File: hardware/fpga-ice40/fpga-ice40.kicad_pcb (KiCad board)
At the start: 4 copper layers, 53.3 x 70.1 mm, 65 parts, among them J1 MicroSD_Molex_1040310811, J2 ProgHeader_iCE40, J3 ProgHeader_Flash_QSPI, J4 Conn_02x20_Odd_Even, J5 USB_B_Micro, U1 iCE40HX4K-TQ144, U2 IS42S16320F-6TL, U3 W25Q32JVSS, U4 W25Q32JVSS, U5 S25FL256SAGMFI01, U6 S25FL256SAGMFI01, U7 FT245RL

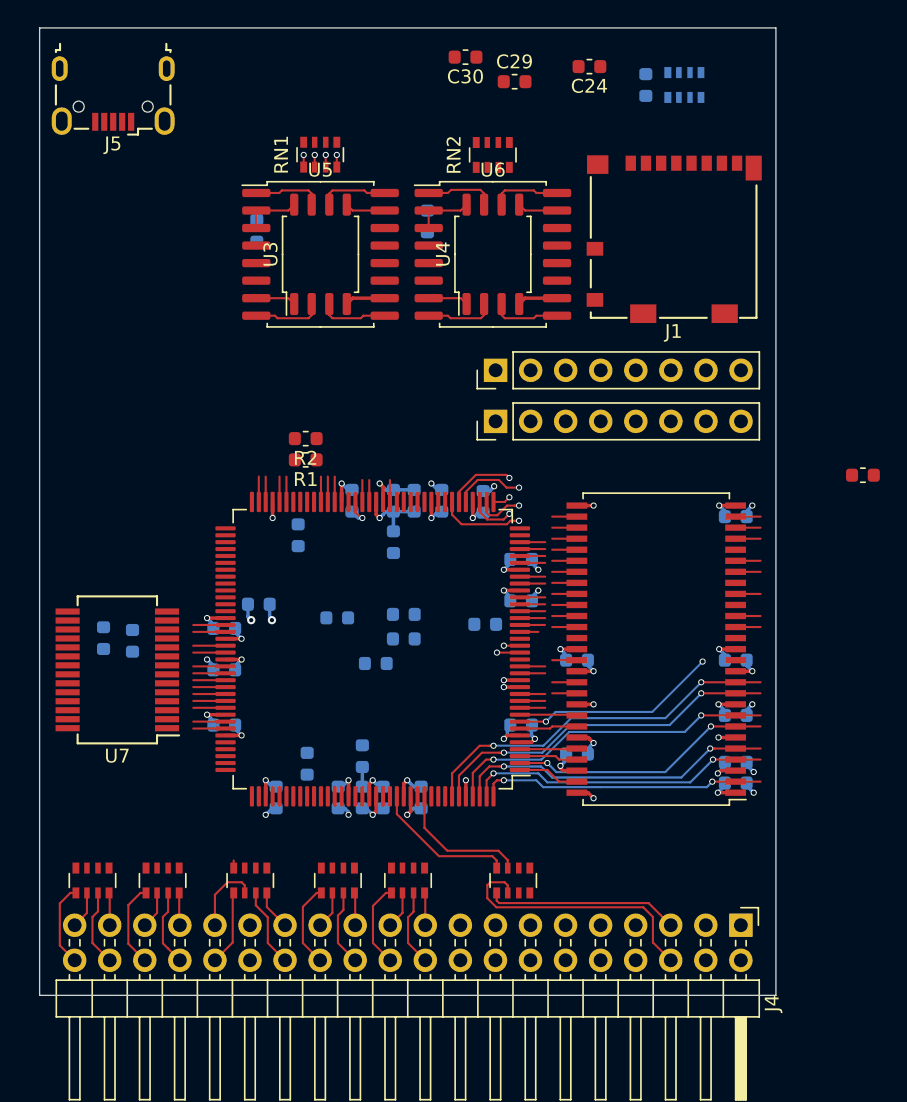
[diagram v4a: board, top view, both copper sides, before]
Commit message: Routing FPGA to SPI flash memory and USB interface
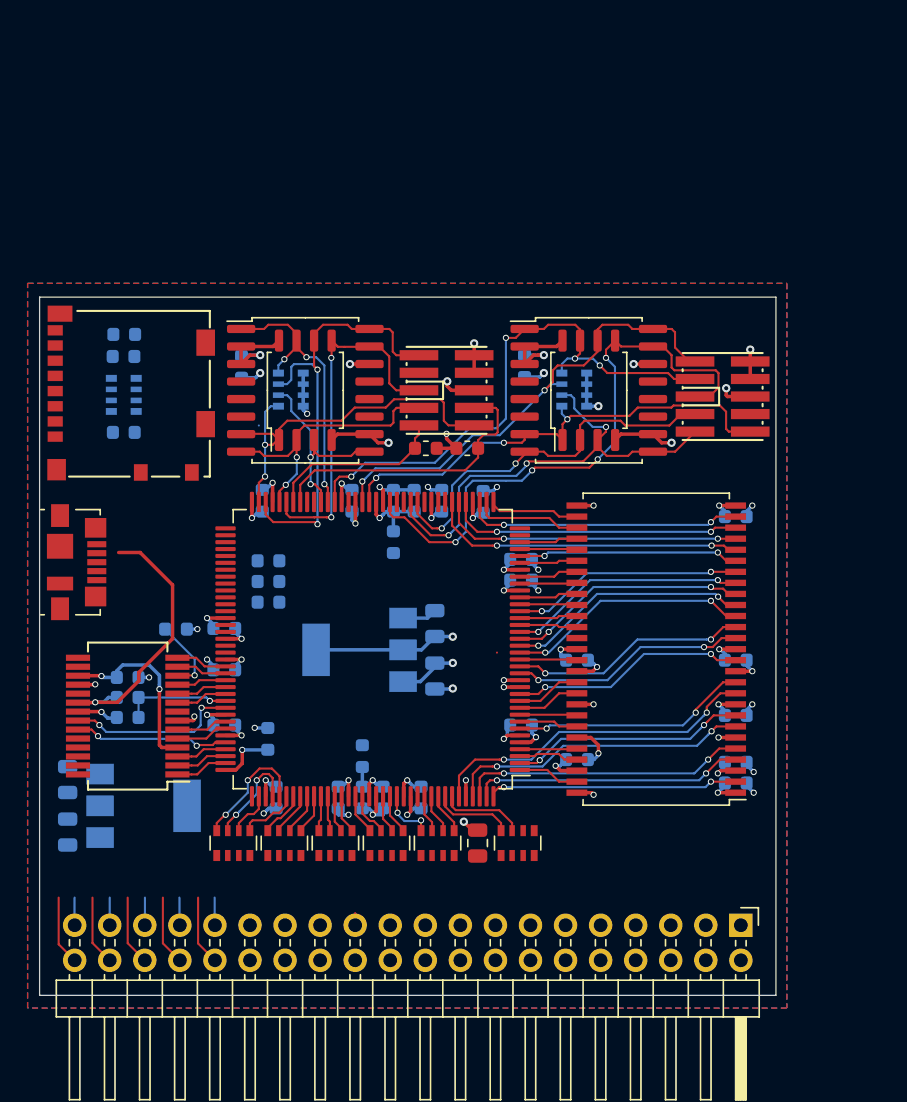
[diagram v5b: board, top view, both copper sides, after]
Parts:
- removed J2: ProgHeader_iCE40, Connector_PinHeader_2.54mm:PinHeader_1x08_P2.54mm_Vertical
- removed J3: ProgHeader_Flash_QSPI, Connector_PinHeader_2.54mm:PinHeader_1x08_P2.54mm_Vertical
- removed R5, R6, R7: 1R, Resistor_SMD:R_0603_1608Metric
- added C34: 10u, Capacitor_SMD:C_0805_2012Metric, B.Cu at (137.9, 104.5)
- added C35: 10u, Capacitor_SMD:C_0805_2012Metric, B.Cu at (137.9, 108.2)
- added C36: 10u, Capacitor_SMD:C_0805_2012Metric, F.Cu at (167.6, 109.0)
- added C37: 10u, Capacitor_SMD:C_0805_2012Metric, B.Cu at (164.5, 97.0)
- added C38: 10u, Capacitor_SMD:C_0805_2012Metric, B.Cu at (164.5, 93.2)
- added J6: Conn_02x05_Odd_Even, ng_conn:Samtec_FTSH-105-XX-X-DV, F.Cu at (165.3, 76.2)
- added J7: Conn_02x05_Odd_Even, ng_conn:Samtec_FTSH-105-XX-X-DV, F.Cu at (185.3, 76.7)
- added U8: AZ1117-1.2, Package_TO_SOT_SMD:SOT-223-3_TabPin2, B.Cu at (143.4, 106.3)
- added U9: AZ1117-1.2, Package_TO_SOT_SMD:SOT-223-3_TabPin2, B.Cu at (159.1, 95.0)
- C24, C30, RN1, RN2: moved to B.Cu
- C28, C29: value 10u -> 100n; moved to B.Cu
- J5: footprint Connector_USB:USB_Micro-B_Wuerth_629105150521 -> Connector_USB:USB_Micro-B_Molex_47346-0001
- R3: value 1R -> 6k8
- R4: value 1R -> 10k
- moved C29 50.9 mm to (152.4, 101.5), turned to 90 degrees
- moved J1 47.8 mm to (137.0, 76.5), turned to 270 degrees
- moved RN3 46.4 mm to (142.0, 76.6), turned to 0 degrees
- moved R8 45.4 mm to (142.0, 79.3), turned to 180 degrees
- moved C28 43.6 mm to (152.0, 84.2), turned to 90 degrees
- moved C24 38.9 mm to (142.0, 72.2), turned to 0 degrees
- moved J5 33.9 mm to (138.6, 88.7), turned to 270 degrees
- moved C30 32.9 mm to (141.9, 73.8), turned to 0 degrees
- moved R3 20.4 mm to (142.2, 98.5)
- moved RN2 18.0 mm to (174.6, 76.2), turned to 0 degrees
- moved RN1 17.2 mm to (154.1, 76.2), turned to 0 degrees
- moved R4 13.4 mm to (142.2, 100.0), turned to 180 degrees
- moved C23 12.6 mm to (171.0, 74.5)
- moved U4 12.1 mm to (175.7, 76.2)
- moved U6 12.1 mm to (175.7, 76.2)
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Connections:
- net N64_VCC renamed N64_3V3
- net Net-(R9-Pad2) renamed /USB_PWRENn
- C1 pad 1: VCCINT -> P1V2
- C10 pad 1: VCCIO1 -> P3V3
- C11 pad 1: VCCIO2 -> P3V3
- C12 pad 1: VCCIO2 -> P3V3
- C13 pad 1: VCCIO3 -> P3V3
- C14 pad 1: VCCIO3 -> P3V3
- C15 pad 1: P3V3_DRAM -> P3V3
- C16 pad 1: P3V3_DRAM -> P3V3
- C17 pad 1: P3V3_DRAM -> P3V3
- C18 pad 1: P3V3_DRAM -> P3V3
- C19 pad 1: P3V3_DRAM -> P3V3
- C2 pad 1: VCCINT -> P1V2
- C20 pad 1: P3V3_DRAM -> P3V3
- C21 pad 1: P3V3_DRAM -> P3V3
- C22 pad 1: P3V3_FLASH -> P3V3
- C23 pad 1: P3V3_FLASH -> P3V3
- C24 pad 1: P3V3_SD -> P3V3
- C27 pad 1: P3V3_FPGA -> P3V3
- C28 pad 1: P3V3_DRAM -> P3V3
- C29 pad 1: P3V3_FLASH -> VCC2V5
- C3 pad 1: VCCINT -> P1V2
- C30 pad 1: P3V3_SD -> P3V3
- C31 pad 1: VCCINT -> P1V2
- C32 pad 1: VCCINT -> P1V2
- C33 pad 1: Net-(C33-Pad1) -> /USB_VIO
- C4 pad 1: VCCINT -> P1V2
- C7 pad 1: VCCIO0 -> P3V3
- C8 pad 1: VCCIO0 -> P3V3
- C9 pad 1: VCCIO1 -> P3V3
- J1 pad 4: P3V3_SD -> P3V3
- R3 pad 1: VCCINT -> USB_VBUS
- R3 pad 2: P1V2 -> USB_DETn
- R4 pad 1: VCCIO0 -> USB_DETn
- R4 pad 2: P3V3 -> GND
- R8 pad 1: P3V3_SD -> P3V3
- RN1 pad 2: CONFIG_SCK -> CONFIG_IO2
- RN1 pad 3: CONFIG_IO2 -> CONFIG_SCK
- RN1 pad 5: P3V3_FLASH -> P3V3
- RN1 pad 6: P3V3_FLASH -> P3V3
- RN1 pad 7: P3V3_FLASH -> P3V3
- RN1 pad 8: P3V3_FLASH -> P3V3
- RN2 pad 2: FLASH_SCK -> FLASH_IO2
- RN2 pad 3: FLASH_IO2 -> FLASH_SCK
- RN2 pad 5: P3V3_FLASH -> P3V3
- RN2 pad 6: P3V3_FLASH -> P3V3
- RN2 pad 7: P3V3_FLASH -> P3V3
- RN2 pad 8: P3V3_FLASH -> P3V3
- RN3 pad 5: P3V3_SD -> P3V3
- RN3 pad 6: P3V3_SD -> P3V3
- RN3 pad 7: P3V3_SD -> P3V3
- RN3 pad 8: P3V3_SD -> P3V3
- U1 pad 10: Net-(U1-Pad10) -> DRAM_DQ10
- U1 pad 100: VCCIO1 -> P3V3
- U1 pad 101: Net-(U1-Pad101) -> FIFO_D7
- U1 pad 102: Net-(U1-Pad102) -> FIFO_D1
- U1 pad 104: N64_AD15_IC -> FIFO_RXFn
- U1 pad 105: N64_AD0_IC -> FIFO_D2
- U1 pad 106: N64_AD14_IC -> FIFO_D4
- U1 pad 107: N64_AD1_IC -> FIFO_D0
- U1 pad 11: Net-(U1-Pad11) -> DRAM_DQ9
- U1 pad 110: N64_AD13_IC -> N64_AD14_IC
- U1 pad 111: VCCINT -> P1V2
- U1 pad 112: N64_AD2_IC -> N64_AD0_IC
- U1 pad 113: N64_AD12_IC -> N64_AD15_IC
- U1 pad 114: N64_AD3_IC -> N64_AD1_IC
- U1 pad 115: N64_WRITEn_IC -> N64_AD13_IC
- U1 pad 116: N64_ALE_L_IC -> N64_AD2_IC
- U1 pad 117: N64_READn_IC -> N64_AD12_IC
- U1 pad 118: N64_ALE_H_IC -> N64_AD3_IC
- U1 pad 119: N64_AD11_IC -> N64_WRITEn_IC
- U1 pad 12: Net-(U1-Pad12) -> DRAM_DQ7
- U1 pad 120: N64_AD4_IC -> N64_ALE_L_IC
- U1 pad 121: N64_AD10_IC -> N64_READn_IC
- U1 pad 122: N64_AD5_IC -> N64_ALE_H_IC
- U1 pad 123: VCCIO0 -> P3V3
- U1 pad 124: N64_AD9_IC -> N64_AD11_IC
- U1 pad 125: N64_AD6_IC -> N64_AD4_IC
- U1 pad 128: N64_AD8_IC -> N64_AD10_IC
- U1 pad 129: N64_AD7_IC -> N64_AD5_IC
- U1 pad 130: N64_COLD_RESETn_IC -> N64_AD9_IC
- U1 pad 131: VCCIO0 -> P3V3
- U1 pad 134: N64_OS_EVENTn_IC -> N64_AD6_IC
- U1 pad 135: Net-(U1-Pad135) -> N64_AD8_IC
- U1 pad 136: Net-(U1-Pad136) -> N64_AD7_IC
- U1 pad 137: Net-(U1-Pad137) -> N64_COLD_RESETn_IC
- U1 pad 138: DRAM_DQ6 -> N64_OS_EVENTn_IC
- U1 pad 141: DRAM_DQ4 -> DRAM_DQ3
- U1 pad 15: DRAM_DQ9 -> DRAM_LDQM
- U1 pad 16: DRAM_DQ8 -> DRAM_WEn
- U1 pad 17: Net-(U1-Pad17) -> DRAM_DQ8
- U1 pad 18: Net-(U1-Pad18) -> DRAM_CASn
- U1 pad 19: Net-(U1-Pad19) -> DRAM_RASn
- U1 pad 2: DRAM_DQ3 -> DRAM_DQ4
- U1 pad 20: Net-(U1-Pad20) -> DRAM_CSn
- U1 pad 21: Net-(U1-Pad21) -> DRAM_BA0
- U1 pad 22: Net-(U1-Pad22) -> DRAM_UDQM
- U1 pad 23: Net-(U1-Pad23) -> DRAM_CLK
- U1 pad 24: Net-(U1-Pad24) -> DRAM_BA1
- U1 pad 25: Net-(U1-Pad25) -> DRAM_CKE
- U1 pad 26: Net-(U1-Pad26) -> DRAM_A12
- U1 pad 27: VCCINT -> P1V2
- U1 pad 28: Net-(U1-Pad28) -> DRAM_A11
- U1 pad 29: Net-(U1-Pad29) -> DRAM_A9
- U1 pad 30: VCCIO3 -> P3V3
- U1 pad 31: Net-(U1-Pad31) -> DRAM_A8
- U1 pad 32: Net-(U1-Pad32) -> DRAM_A10
- U1 pad 33: Net-(U1-Pad33) -> DRAM_A7
- U1 pad 34: Net-(U1-Pad34) -> DRAM_A6
- U1 pad 37: Net-(U1-Pad37) -> DRAM_A4
- U1 pad 38: Net-(U1-Pad38) -> DRAM_A5
- U1 pad 39: Net-(U1-Pad39) -> DRAM_A3
- U1 pad 40: VCCINT -> P1V2
- U1 pad 41: Net-(U1-Pad41) -> DRAM_A2
- U1 pad 42: Net-(U1-Pad42) -> DRAM_A1
- U1 pad 43: Net-(U1-Pad43) -> DRAM_A0
- U1 pad 46: VCCIO2 -> P3V3
- U1 pad 48: FLASH_SSn -> FLASH_MISO|IO1
- U1 pad 49: FLASH_SCK -> FLASH_IO2
- U1 pad 55: FLASH_MISO|IO1 -> FLASH_SSn
- U1 pad 56: FLASH_IO2 -> FLASH_SCK
- U1 pad 57: VCCIO2 -> P3V3
- U1 pad 6: VCCIO3 -> P3V3
- U1 pad 7: DRAM_DQ12 -> DRAM_DQ6
- U1 pad 72: VCCSPI -> P3V3
- U1 pad 8: Net-(U1-Pad8) -> DRAM_DQ12
- U1 pad 89: VCCIO1 -> P3V3
- U1 pad 92: VCCINT -> P1V2
- U1 pad 93: Net-(U1-Pad93) -> FIFO_WR
- U1 pad 94: Net-(U1-Pad94) -> FIFO_RDn
- U1 pad 95: Net-(U1-Pad95) -> FIFO_D3
- U1 pad 96: Net-(U1-Pad96) -> FIFO_D6
- U1 pad 97: Net-(U1-Pad97) -> FIFO_D5
- U1 pad 98: Net-(U1-Pad98) -> USB_DETn
- U1 pad 99: Net-(U1-Pad99) -> FIFO_TXEn
- U2 pad 1: P3V3_DRAM -> P3V3
- U2 pad 14: P3V3_DRAM -> P3V3
- U2 pad 27: P3V3_DRAM -> P3V3
- U2 pad 3: P3V3_DRAM -> P3V3
- U2 pad 43: P3V3_DRAM -> P3V3
- U2 pad 49: P3V3_DRAM -> P3V3
- U2 pad 9: P3V3_DRAM -> P3V3
- U3 pad 8: P3V3_FLASH -> P3V3
- U4 pad 8: P3V3_FLASH -> P3V3
- U5 pad 14: P3V3_FLASH -> P3V3
- U5 pad 2: P3V3_FLASH -> P3V3
- U5 pad 3: P3V3_FLASH -> P3V3
- U6 pad 14: P3V3_FLASH -> P3V3
- U6 pad 2: P3V3_FLASH -> P3V3
- U6 pad 3: P3V3_FLASH -> P3V3
- U7 pad 17: Net-(C33-Pad1) -> /USB_VIO
- U7 pad 19: Net-(U7-Pad19) -> USB_DETn
- U7 pad 4: P3V3 -> /USB_VIO
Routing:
- net P3V3: track 1.22 -> 73.9 mm, vias 1 -> 27
- net FLASH_MOSI|IO0: track 4.51 -> 42.8 mm, vias 0 -> 4
- net FLASH_IO3: track 6.86 -> 41.6 mm, vias 0 -> 4
- net FLASH_SSn: track 2.92 -> 35.1 mm, vias 0 -> 3
- net FLASH_SCK: track 4.99 -> 34.9 mm, vias 0 -> 2
- net FLASH_IO2: track 6.57 -> 35.2 mm, vias 0 -> 3
- net CONFIG_SCK: track 7.71 -> 32.6 mm, vias 1 -> 2
- net GND: track 44.5 -> 69.3 mm, vias 27 -> 40
- net CONFIG_SSn: track 5.64 -> 29.3 mm, vias 1 -> 2
- net DRAM_A0: track 0.00 -> 23.0 mm, vias 0 -> 2
- net CONFIG_MOSI|IO0: track 4.76 -> 27.7 mm, vias 0 -> 2
- net FLASH_MISO|IO1: track 6.57 -> 28.8 mm, vias 0 -> 2
- net FPGA_CDONE: track 0.00 -> 21.2 mm
- net DRAM_A1: track 1.81 -> 22.0 mm, vias 0 -> 2
- net USB_VBUS: track 0.00 -> 19.6 mm, vias 0 -> 1
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- added copper zone on B.Cu, net GND
- added copper zone on F.Cu, net GND
- added copper zone on In2(PWR).Cu, net P3V3
- removed copper zone on In2(PWR).Cu, net P1V2
- removed copper zone on In2(PWR).Cu, net P3V3_FPGA
- removed copper zone on In2(PWR).Cu, net VCCIO0
- removed copper zone on In2(PWR).Cu, net VCCIO1
- removed copper zone on In2(PWR).Cu, net VCCIO2
- removed copper zone on In2(PWR).Cu, net VCCIO3
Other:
- board size 53.3 x 70.1 mm -> 53.3 x 50.6 mm
- rule pad_to_mask_clearance: 0.051 -> 0.05

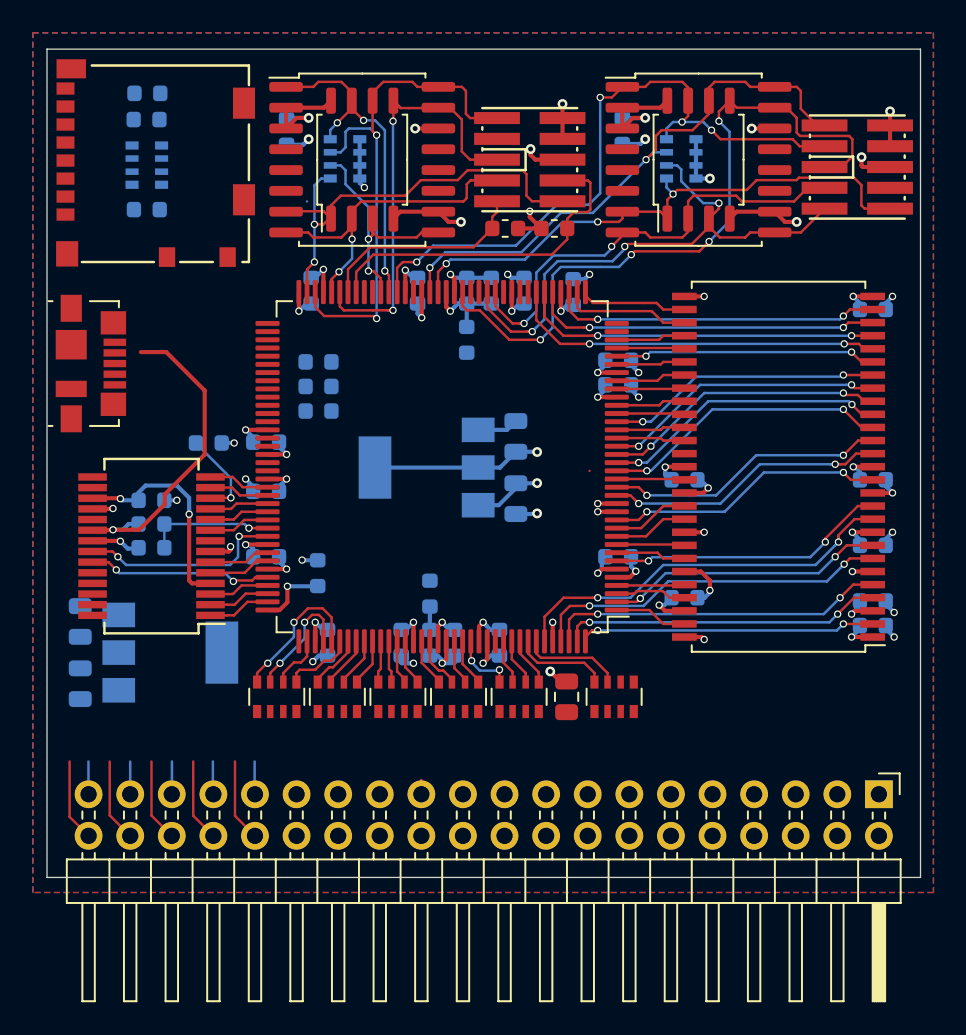
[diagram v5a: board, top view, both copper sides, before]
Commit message: Oscillator, LEDs implemented, with all traces routed roughly
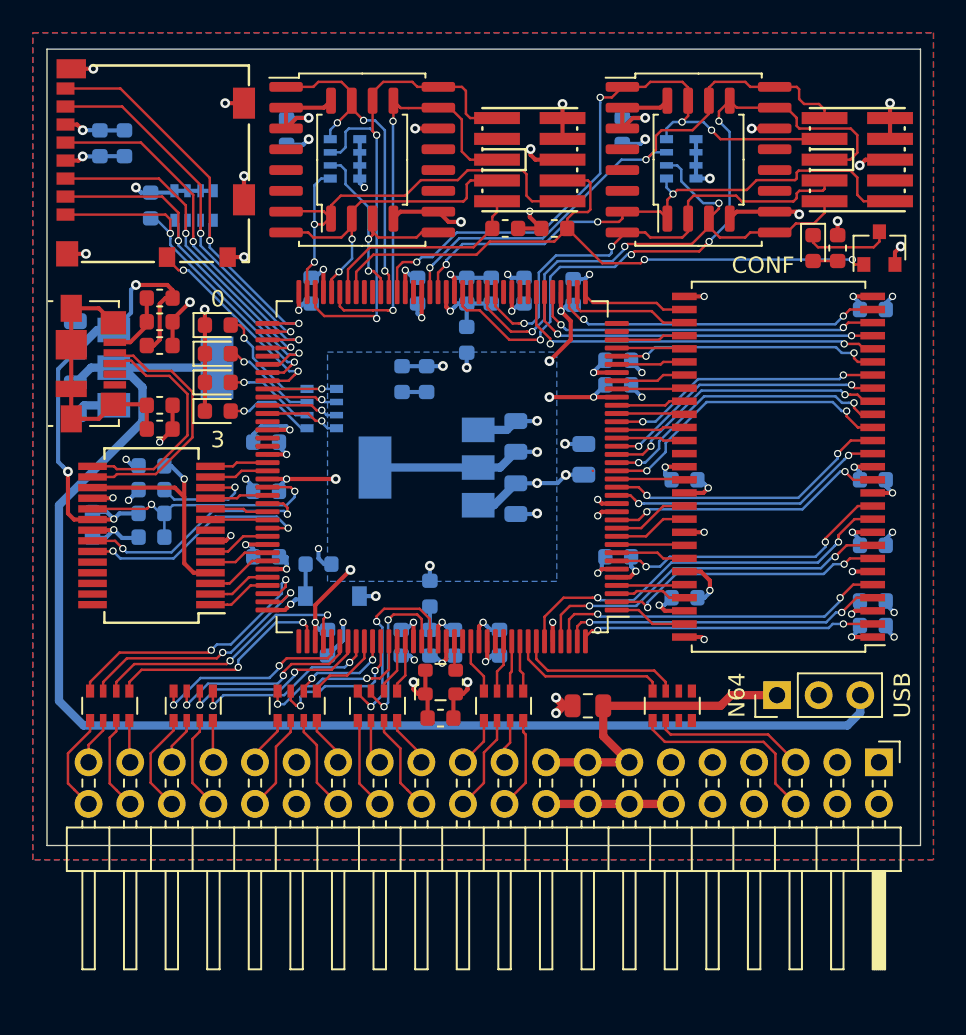
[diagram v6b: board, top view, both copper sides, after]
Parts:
- added C39: 10n, Capacitor_SMD:C_0603_1608Metric, F.Cu at (142.8, 86.2)
- added C40: 10n, Capacitor_SMD:C_0603_1608Metric, B.Cu at (138.7, 98.5)
- added C41: 100n, Capacitor_SMD:C_0603_1608Metric, F.Cu at (142.8, 87.6)
- added C42: 10n, Capacitor_SMD:C_0603_1608Metric, F.Cu at (142.8, 91.2)
- added C43: 100n, Capacitor_SMD:C_0603_1608Metric, F.Cu at (159.9, 110.3)
- added D1: ~~800mVf, Diode_SMD:D_SOD-123, B.Cu at (153.3, 102.9)
- added D2: Blue, LED_SMD:LED_0603_1608Metric, F.Cu at (182.7, 81.7)
- added D3: Blue, LED_SMD:LED_0603_1608Metric, F.Cu at (146.3, 86.3)
- added D4: Blue, LED_SMD:LED_0603_1608Metric, F.Cu at (146.3, 88.1)
- added D5: Blue, LED_SMD:LED_0603_1608Metric, F.Cu at (146.3, 89.8)
- added D6: Blue, LED_SMD:LED_0603_1608Metric, F.Cu at (146.3, 91.6)
- added FB1: 33R, 500mA, Inductor_SMD:L_0603_1608Metric, F.Cu at (142.8, 84.7)
- added J2: Conn_01x03, Connector_PinHeader_2.54mm:PinHeader_1x03_P2.54mm_Vertical, F.Cu at (180.4, 109.0)
- added Q1: 2N7002H, Package_TO_SOT_SMD:SOT-23, F.Cu at (186.7, 81.7)
- added R5: 470R, Resistor_SMD:R_0603_1608Metric, F.Cu at (184.2, 81.7)
- added R6: 100k, Resistor_SMD:R_0603_1608Metric, F.Cu at (142.8, 92.7)
- added R7: 330R, Resistor_SMD:R_Array_Convex_4x0603, B.Cu at (152.7, 91.5)
- added X1: ECS-2520MV-xxx-xx, Oscillator:Oscillator_SMD_ECS_2520MV-xxx-xx-4Pin_2.5x2.0mm, F.Cu at (159.9, 108.2)
- C27: footprint Capacitor_SMD:C_0603_1608Metric -> Capacitor_SMD:C_0805_2012Metric
- RN4, RN5, RN6, RN7, RN8, RN9: value 33R0 -> 33R
- moved C34 17.4 mm to (137.6, 87.0)
- moved C35 17.4 mm to (137.6, 90.8)
- moved U8 17.4 mm to (143.1, 89.0)
- moved C27 17.3 mm to (168.7, 94.5), turned to 90 degrees
- moved RN4 10.2 mm to (139.7, 109.6)
- moved RN5 8.82 mm to (144.8, 109.6)
- moved C32 6.88 mm to (159.1, 89.7), turned to 90 degrees
- moved RN6 6.17 mm to (151.2, 109.6)
- moved C31 5.12 mm to (157.6, 89.7), turned to 90 degrees
- moved RN7 4.98 mm to (156.1, 109.6)
- moved R9 4.51 mm to (142.2, 96.4), turned to 0 degrees
- moved C24 4.21 mm to (139.1, 75.2), turned to 90 degrees
- moved RN3 3.80 mm to (144.8, 79.0), turned to 90 degrees
- moved RN9 3.59 mm to (174.1, 109.6)
- moved C33 2.10 mm to (142.2, 95.0), turned to 180 degrees
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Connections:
- C34 pad 1: USB_VBUS -> USB_5V
- J1 pad 9: Net-(J1-Pad9) -> SD_CD
- J5 pad 1: USB_VBUS -> /USB_VBUS
- J5 pad 6: Net-(J5-Pad6) -> /USB_SHD
- R3 pad 1: USB_VBUS -> USB_5V
- RN3 pad 1: SD_DAT3 -> SD_DAT1
- RN3 pad 2: SD_CMD -> SD_DAT0
- RN3 pad 3: SD_DAT0 -> SD_CMD
- RN3 pad 4: SD_DAT1 -> SD_DAT3
- RN6 pad 1: N64_WRITEn -> N64_ALE_L
- RN6 pad 2: N64_ALE_L -> N64_WRITEn
- RN6 pad 7: N64_ALE_L_IC -> N64_WRITEn_IC
- RN6 pad 8: N64_WRITEn_IC -> N64_ALE_L_IC
- RN8 pad 1: N64_AD9 -> N64_AD6
- RN8 pad 2: N64_AD6 -> N64_AD9
- RN8 pad 3: N64_AD8 -> N64_AD7
- RN8 pad 4: N64_AD7 -> N64_AD8
- RN8 pad 5: N64_AD7_IC -> N64_AD8_IC
- RN8 pad 6: N64_AD8_IC -> N64_AD7_IC
- RN8 pad 7: N64_AD6_IC -> N64_AD9_IC
- RN8 pad 8: N64_AD9_IC -> N64_AD6_IC
- RN9 pad 1: N64_COLD_RESETn -> N64_OS_EVENTn
- RN9 pad 2: N64_OS_EVENTn -> N64_COLD_RESETn
- RN9 pad 7: N64_OS_EVENTn_IC -> N64_COLD_RESETn_IC
- RN9 pad 8: N64_COLD_RESETn_IC -> N64_OS_EVENTn_IC
- U1 pad 101: FIFO_D7 -> FIFO_D1
- U1 pad 102: FIFO_D1 -> FIFO_D2
- U1 pad 104: FIFO_RXFn -> FIFO_D4
- U1 pad 105: FIFO_D2 -> FIFO_D0
- U1 pad 106: FIFO_D4 -> N64_AD15_IC
- U1 pad 107: FIFO_D0 -> N64_AD0_IC
- U1 pad 110: N64_AD14_IC -> N64_AD1_IC
- U1 pad 112: N64_AD0_IC -> N64_AD14_IC
- U1 pad 113: N64_AD15_IC -> N64_AD13_IC
- U1 pad 114: N64_AD1_IC -> N64_AD2_IC
- U1 pad 115: N64_AD13_IC -> N64_AD12_IC
- U1 pad 116: N64_AD2_IC -> N64_AD3_IC
- U1 pad 117: N64_AD12_IC -> N64_ALE_H_IC
- U1 pad 118: N64_AD3_IC -> N64_READn_IC
- U1 pad 121: N64_READn_IC -> N64_AD10_IC
- U1 pad 122: N64_ALE_H_IC -> N64_AD5_IC
- U1 pad 124: N64_AD11_IC -> N64_AD4_IC
- U1 pad 125: N64_AD4_IC -> N64_AD11_IC
- U1 pad 128: N64_AD10_IC -> CLK_50MHZ
- U1 pad 129: N64_AD5_IC -> Net-(U1-Pad129)
- U1 pad 130: N64_AD9_IC -> N64_AD6_IC
- U1 pad 134: N64_AD6_IC -> N64_AD9_IC
- U1 pad 135: N64_AD8_IC -> N64_AD7_IC
- U1 pad 136: N64_AD7_IC -> N64_AD8_IC
- U1 pad 137: N64_COLD_RESETn_IC -> N64_OS_EVENTn_IC
- U1 pad 138: N64_OS_EVENTn_IC -> N64_COLD_RESETn_IC
- U1 pad 141: DRAM_DQ3 -> DRAM_DQ4
- U1 pad 2: DRAM_DQ4 -> DRAM_DQ3
- U1 pad 73: Net-(U1-Pad73) -> SD_DAT1
- U1 pad 74: Net-(U1-Pad74) -> SD_DAT0
- U1 pad 75: Net-(U1-Pad75) -> SD_CLK
- U1 pad 76: Net-(U1-Pad76) -> SD_CMD
- U1 pad 78: Net-(U1-Pad78) -> SD_DAT3
- U1 pad 79: Net-(U1-Pad79) -> SD_DAT2
- U1 pad 80: Net-(U1-Pad80) -> SD_CD
- U1 pad 81: Net-(U1-Pad81) -> LED_D0
- U1 pad 82: Net-(U1-Pad82) -> LED_D1
- U1 pad 83: Net-(U1-Pad83) -> LED_D2
- U1 pad 84: Net-(U1-Pad84) -> LED_D3
- U1 pad 90: Net-(U1-Pad90) -> FIFO_WR
- U1 pad 91: Net-(U1-Pad91) -> FIFO_RDn
- U1 pad 93: FIFO_WR -> USB_DETn
- U1 pad 94: FIFO_RDn -> FIFO_D3
- U1 pad 95: FIFO_D3 -> FIFO_TXEn
- U1 pad 98: USB_DETn -> FIFO_RXFn
- U1 pad 99: FIFO_TXEn -> FIFO_D7
- U7 pad 20: USB_VBUS -> USB_5V
- U8 pad 3: USB_VBUS -> USB_5V
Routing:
- net USB_3V3: track 0.00 -> 83.5 mm
- net GND: track 69.3 -> 117.1 mm, vias 40 -> 55
- net USB_5V: track 0.00 -> 29.8 mm, vias 0 -> 3
- net SD_DAT1: track 0.00 -> 25.9 mm, vias 0 -> 2
- net SD_DAT0: track 0.00 -> 23.8 mm, vias 0 -> 2
- net SD_DAT3: track 0.00 -> 23.0 mm, vias 0 -> 2
- net SD_CLK: track 0.00 -> 23.0 mm, vias 0 -> 2
- net SD_DAT2: track 0.00 -> 22.2 mm, vias 0 -> 2
- net SD_CMD: track 0.00 -> 21.7 mm, vias 0 -> 2
- net N64_3V3: track 0.00 -> 20.1 mm
- net USB_VBUS: track 19.6 -> 0.00 mm, vias 1 -> 0
- net FPGA_CDONE: track 21.2 -> 40.2 mm, vias 0 -> 2
- net P3V3: track 73.9 -> 92.0 mm, vias 27 -> 33
- net P1V2: track 18.5 -> 35.9 mm, vias 5 -> 11
- net /USB_SHD: track 0.00 -> 16.1 mm
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- added copper zone on B.Cu, net P1V2
- added copper zone on In2(PWR).Cu, net P1V2
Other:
- board size 53.3 x 50.6 mm -> 53.3 x 48.6 mm
- net class USBD added: clearance 0.1524, trace_width 0.1524, via_dia 0.45, via_drill 0.3
- board text added: "0"
- board text added: "3"
- board text added: "CONF"
- board text added: "N64"
- board text added: "USB"

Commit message: Reroute N64 AD cart net away from clock oscillator output net
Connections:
- U1 pad 128: CLK_50MHZ -> Net-(U1-Pad128)
- U1 pad 129: Net-(U1-Pad129) -> CLK_50MHZ
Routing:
- net N64_AD6_IC: track 3.37 -> 10.7 mm, vias 0 -> 2
